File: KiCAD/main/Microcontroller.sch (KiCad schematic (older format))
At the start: 11 parts

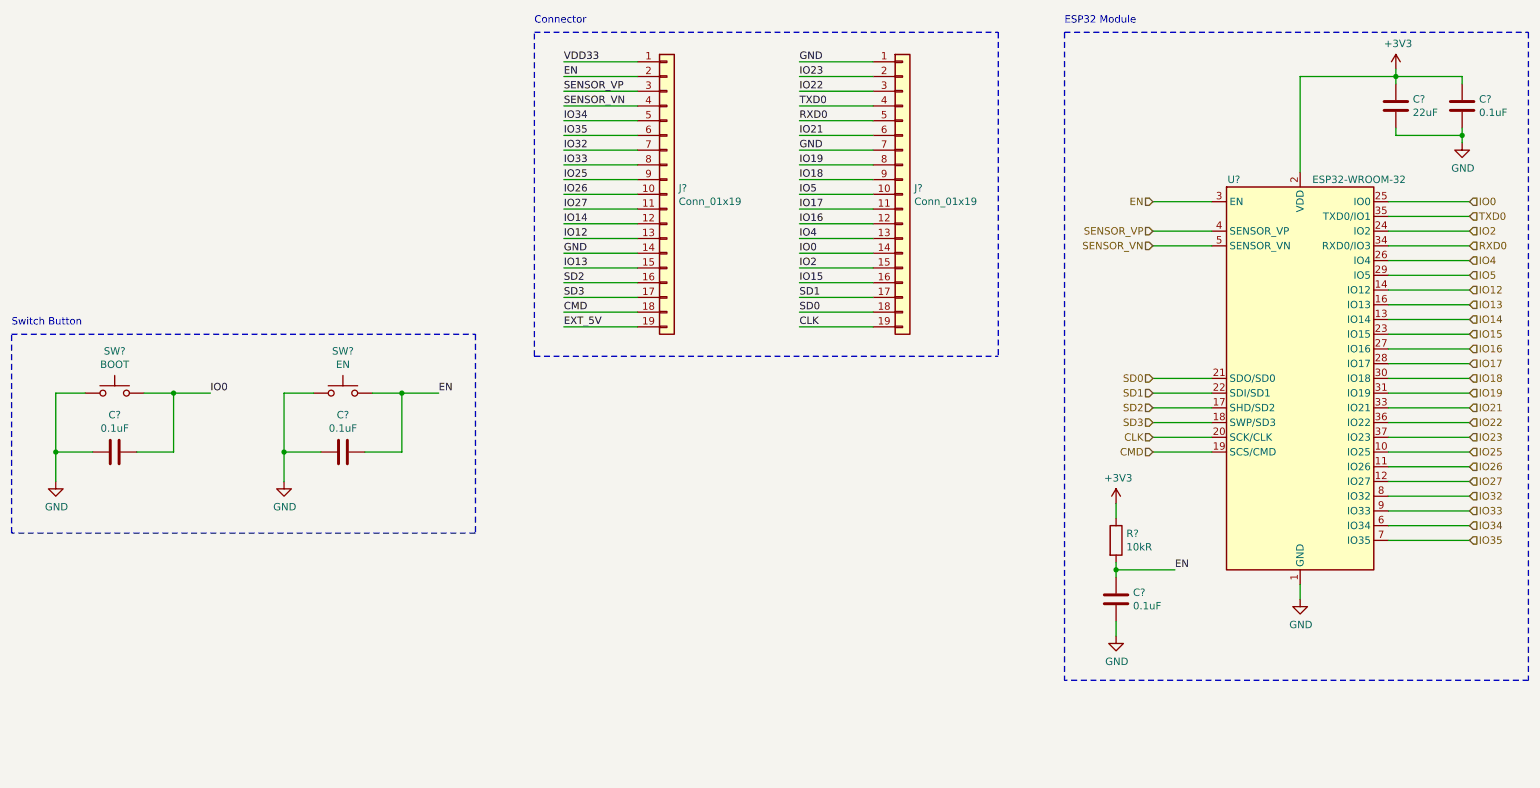
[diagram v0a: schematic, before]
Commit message: Remove unneded header
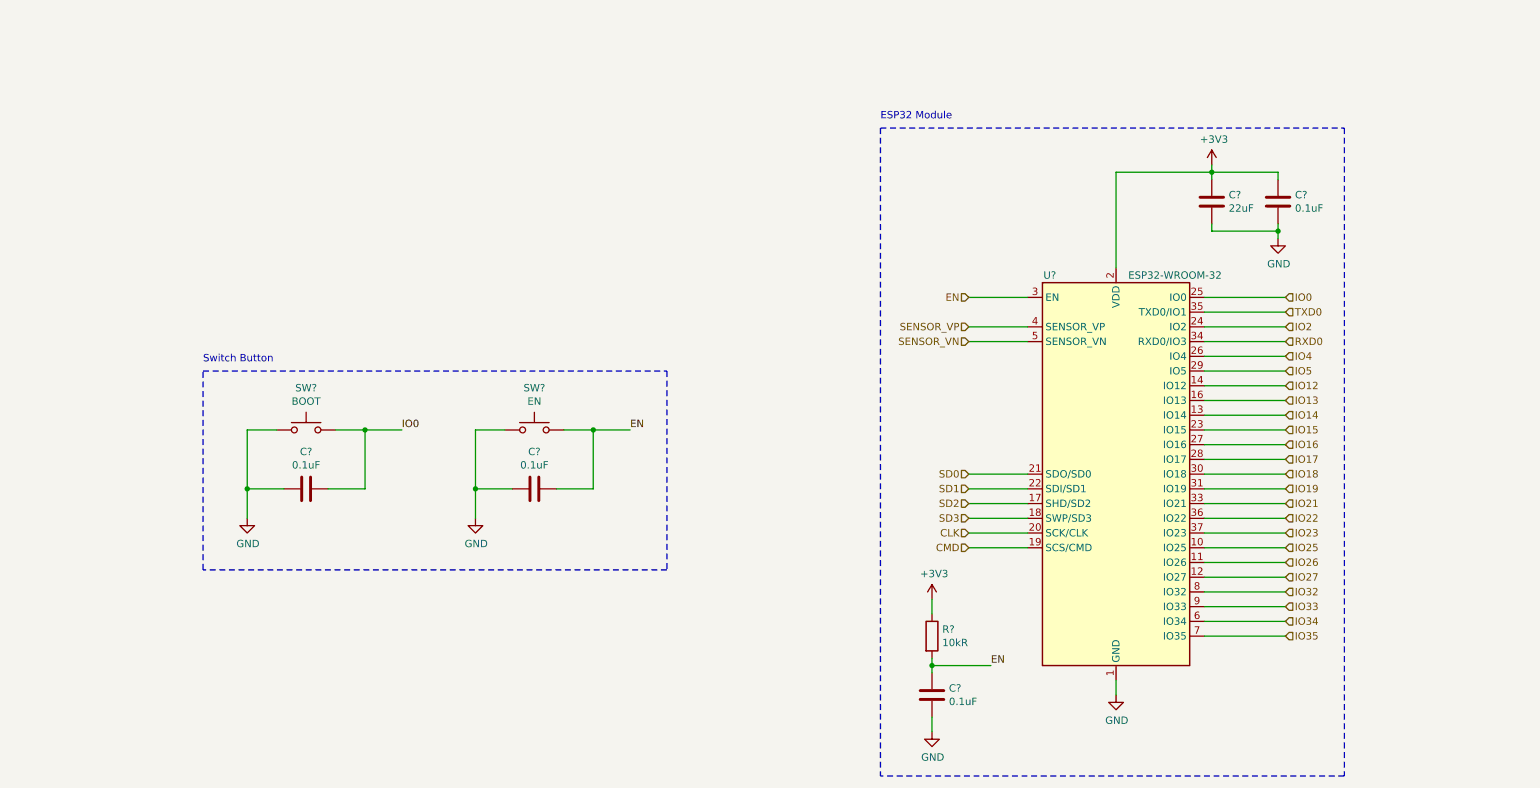
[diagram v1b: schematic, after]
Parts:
- removed J? (x2): Conn_01x19, symbol Connector_Generic:Conn_01x19
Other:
- note removed: "Connector"
- moved on the sheet: C?, R?, SW?, U?

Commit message: Include missing VDD33 label on the microcontroller schematics
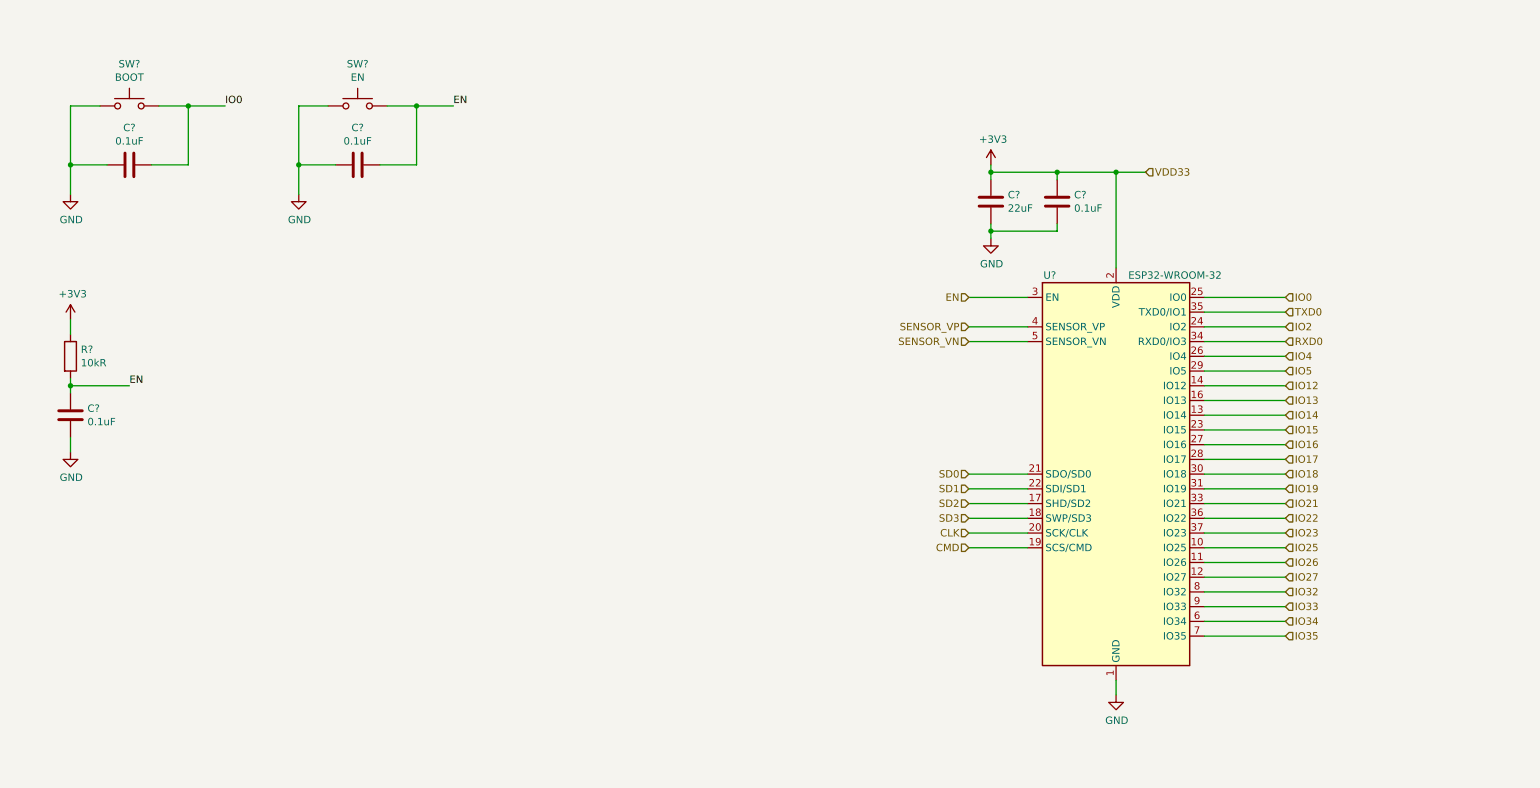
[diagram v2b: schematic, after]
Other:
- note removed: "ESP32 Module"
- note removed: "Switch Button"
- moved on the sheet: C?, R?, SW?

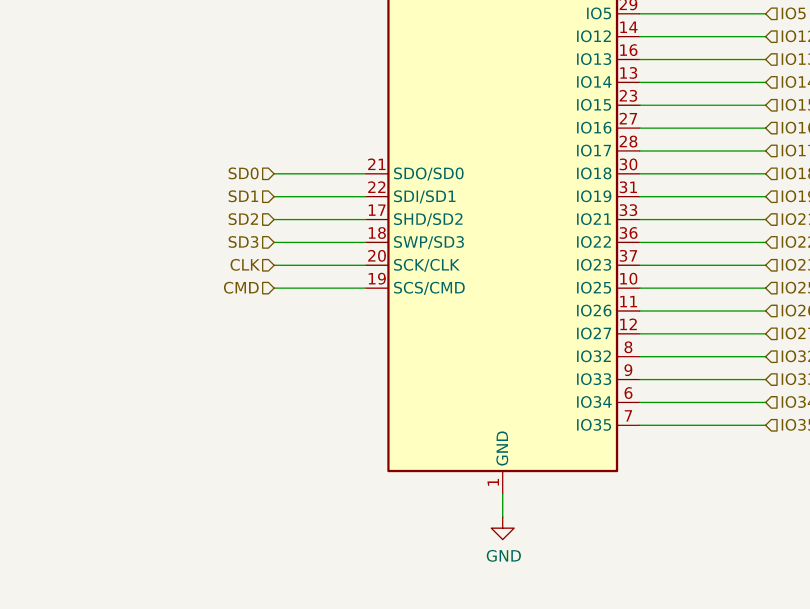
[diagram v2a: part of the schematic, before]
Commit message: Add missing GND label on the microcontroller
and move unneded signals and signals that should not be normally accessible as NC pins
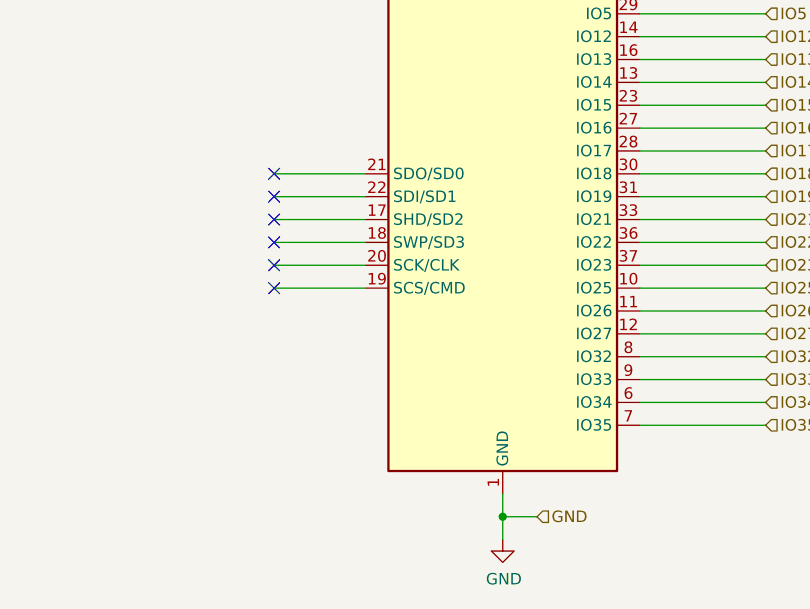
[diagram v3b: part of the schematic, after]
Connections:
- net CLK: no longer names the net of U?.20 (SCK/CLK)
- net CMD: no longer names the net of U?.19 (SCS/CMD)
- net SD0: no longer names the net of U?.21 (SDO/SD0)
- net SD1: no longer names the net of U?.22 (SDI/SD1)
- net SD2: no longer names the net of U?.17 (SHD/SD2)
- net SD3: no longer names the net of U?.18 (SWP/SD3)
- no-connect marks 0 -> 6
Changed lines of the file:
@@
 L power:GND #PWR?
 U 1 1 5F95286C
-P 8200 5200
-F 0 "#PWR?" H 8200 4950 50  0001 C CNN
-F 1 "GND" H 8205 5027 50  0000 C CNN
-F 2 "" H 8200 5200 50  0001 C CNN
-F 3 "" H 8200 5200 50  0001 C CNN
-	1    8200 5200
-	1    0    0    -1
-$EndComp
-Wire Wire Line
-	8200 5100 8200 5200
+P 8200 5300
+F 0 "#PWR?" H 8200 5050 50  0001 C CNN
+F 1 "GND" H 8205 5127 50  0000 C CNN
+F 2 "" H 8200 5300 50  0001 C CNN
+F 3 "" H 8200 5300 50  0001 C CNN
+	1    8200 5300
+	1    0    0    -1
+$EndComp
 Wire Wire Line
 	8800 2600 9350 2600
@@
 Text HLabel 7200 2800 0    50   Input ~ 0
 SENSOR_VN
-Text HLabel 7200 3700 0    50   Input ~ 0
-SD0
-Text HLabel 7200 3800 0    50   Input ~ 0
-SD1
-Text HLabel 7200 3900 0    50   Input ~ 0
-SD2
-Text HLabel 7200 4000 0    50   Input ~ 0
-SD3
-Text HLabel 7200 4100 0    50   Input ~ 0
-CLK
-Text HLabel 7200 4200 0    50   Input ~ 0
-CMD
 Wire Wire Line
 	7600 2700 7200 2700
 Wire Wire Line
 	7200 2800 7600 2800
-Wire Wire Line
-	7600 3700 7200 3700
-Wire Wire Line
-	7600 3800 7200 3800
-Wire Wire Line
-	7600 3900 7200 3900
-Wire Wire Line
-	7600 4000 7200 4000
-Wire Wire Line
-	7600 4100 7200 4100
-Wire Wire Line
-	7600 4200 7200 4200
-Text HLabel 7200 2500 0    50   Input ~ 0
-EN
 Wire Wire Line
 	7200 2500 7600 2500
@@
 	7800 1650 8200 1650
 Connection ~ 8200 1650
+Wire Wire Line
+	7600 4200 7200 4200
+Wire Wire Line
+	7600 4100 7200 4100
+Wire Wire Line
+	7600 4000 7200 4000
+Wire Wire Line
+	7600 3900 7200 3900
+Wire Wire Line
+	7600 3800 7200 3800
+Wire Wire Line
+	7600 3700 7200 3700
+NoConn ~ 7200 3700
+NoConn ~ 7200 3800
+NoConn ~ 7200 3900
+NoConn ~ 7200 4000
+NoConn ~ 7200 4100
+NoConn ~ 7200 4200
+Wire Wire Line
+	8200 5100 8200 5200
+Wire Wire Line
+	8200 5200 8350 5200
+Connection ~ 8200 5200
+Wire Wire Line
+	8200 5200 8200 5300
+Text HLabel 8350 5200 2    50   Input ~ 0
+GND
+Text HLabel 7200 2500 0    50   Input ~ 0
+EN
 $EndSCHEMATC
